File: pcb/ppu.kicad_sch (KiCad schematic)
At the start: 26 parts, among them IC6 AT25SF041B-SSHB-B, J10 Micro_SD_Card_Det2, Q8 MMBT2222A, U5 STM32U073CCUx, Y4 CM7V-T1A-32.768KHZ

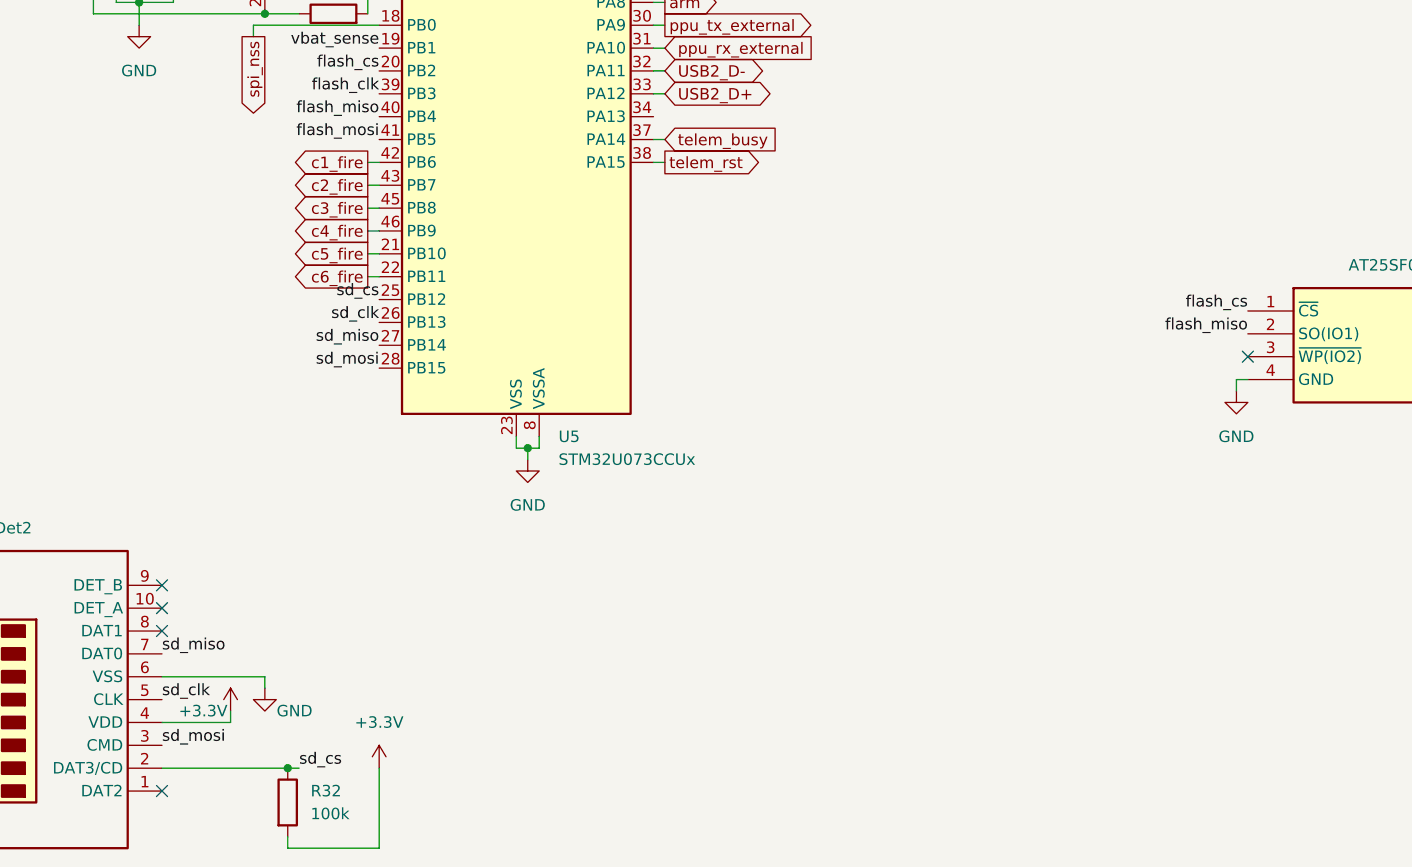
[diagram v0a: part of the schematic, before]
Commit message: lots of work on ppu firmware, especially relating to flash - also corrected some schematic errors (haven't gotten around to updating pcb yet)
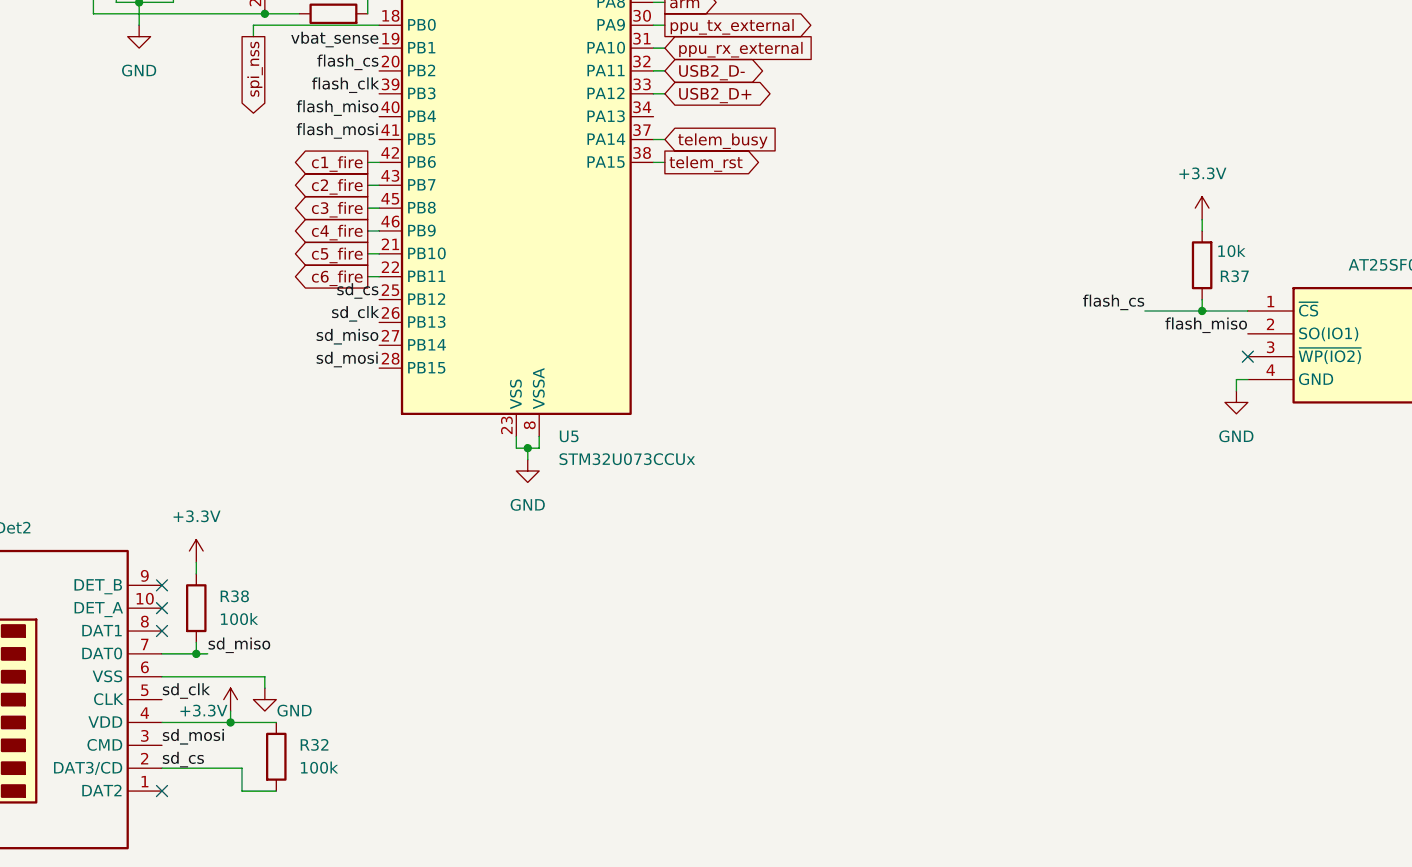
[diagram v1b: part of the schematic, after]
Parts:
- added R37: 10k, Resistor_SMD:R_0402_1005Metric, symbol Device:R
- added R38: 100k, Resistor_SMD:R_0402_1005Metric, symbol Device:R
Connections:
- net +3.3V: now also R32.1, R37.2, R38.1; no longer R32.2
- net flash_cs: now also R37.1
- net sd_cs: now also R32.2; no longer R32.1
- net sd_miso: now also R38.2
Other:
- moved on the sheet: R32

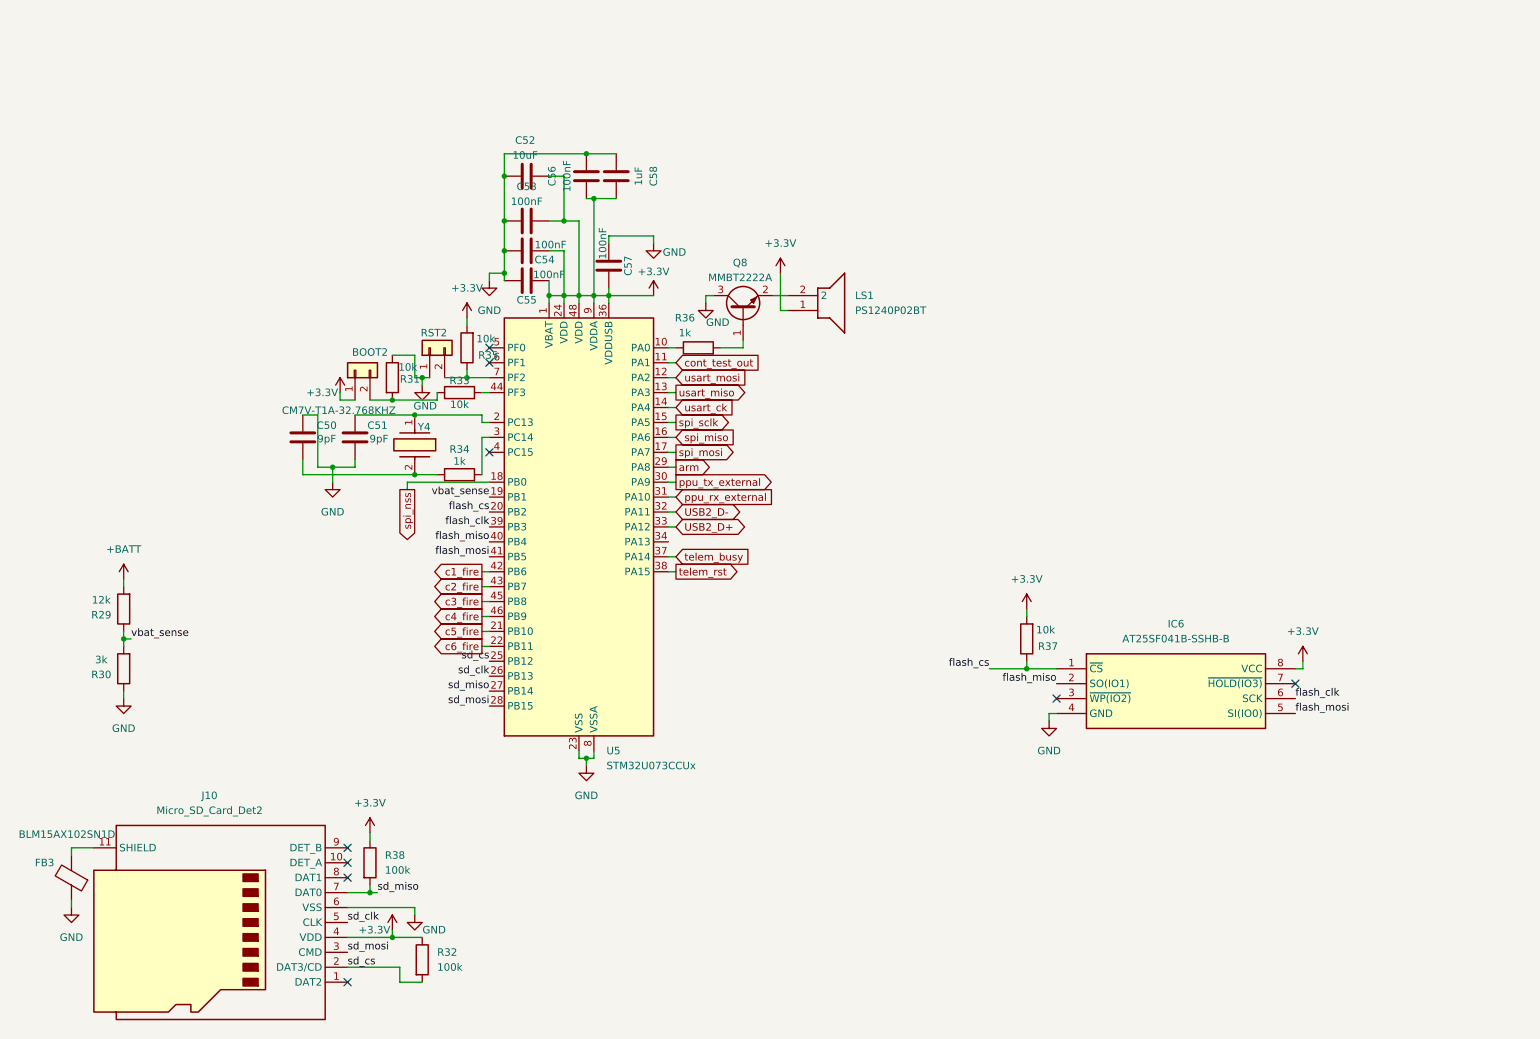
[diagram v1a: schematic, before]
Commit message: reorganized schematic, started to add a readme (not really though), also pcb updated
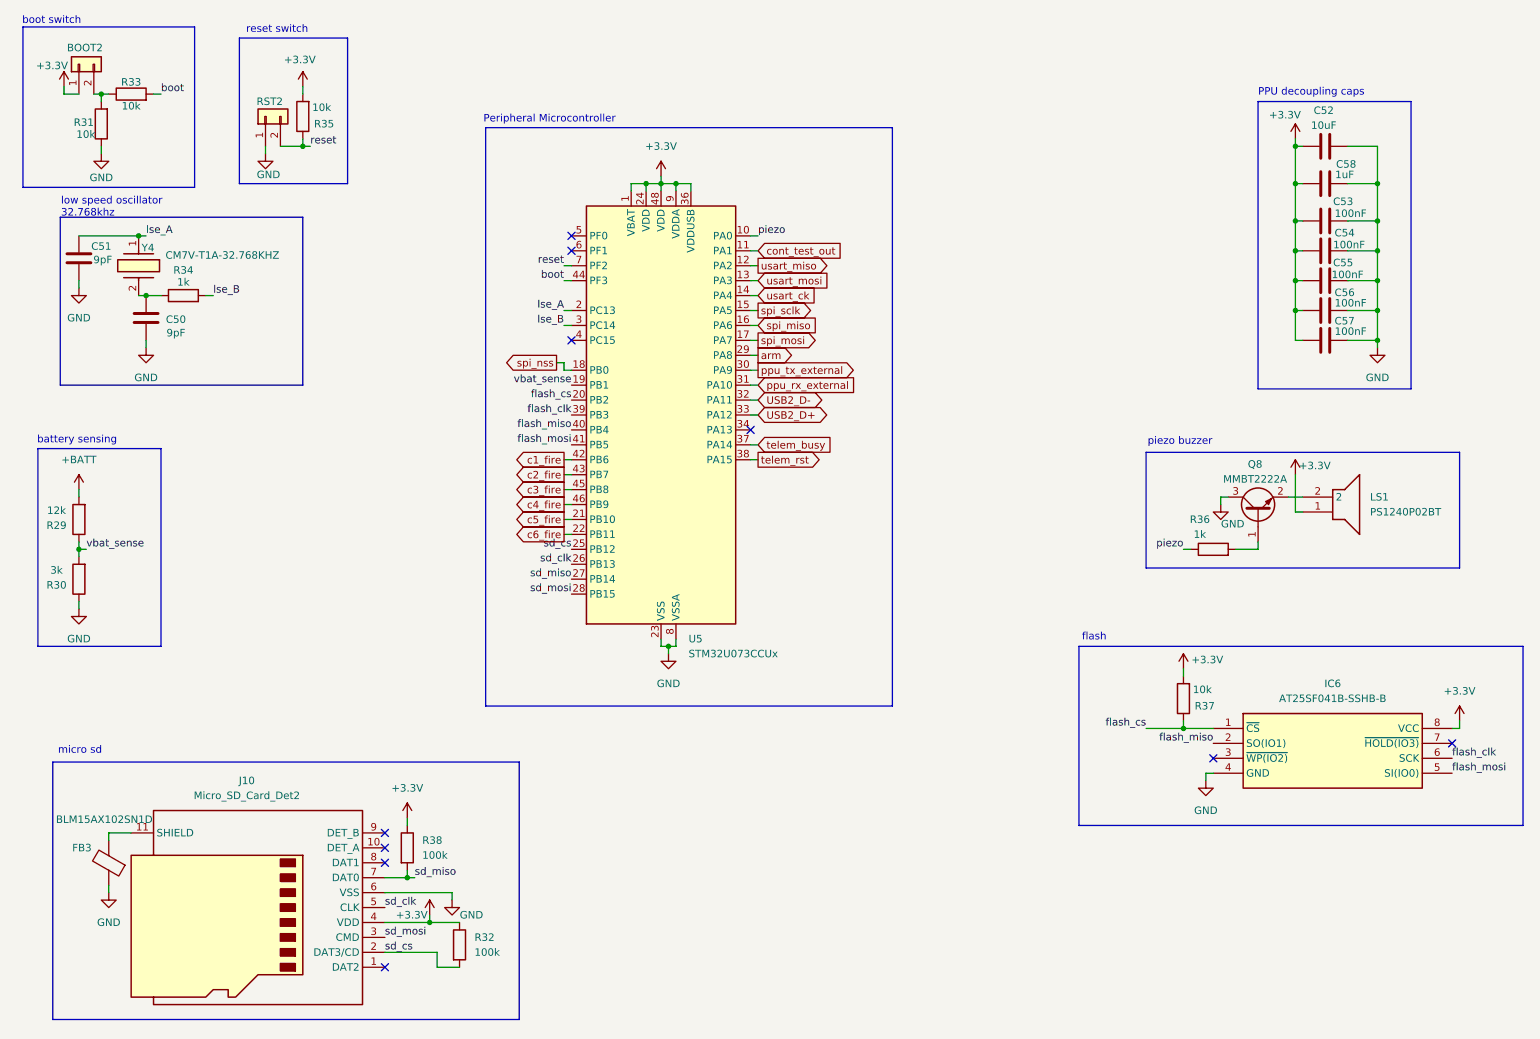
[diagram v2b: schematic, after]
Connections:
- net +3.3V: now also C52.1, C53.1, C54.2, C55.2, C56.2, C57.1, C58.1; no longer C52.2, C53.2, C54.1, C55.1, C56.1, C57.2, C58.2
- net GND: now also C50.2, C52.2, C53.2, C54.1, C55.1, C56.1, C57.2, C58.2; no longer C50.1, C52.1, C53.1, C54.2, C55.2, C56.2, C57.1, C58.1
- net usart_miso: now also U5.12 (PA2); no longer U5.13 (PA3)
- net usart_mosi: now also U5.13 (PA3); no longer U5.12 (PA2)
- net at R34.1, Y4.2: now also C50.1; no longer C50.2
- net reset: now reaches R35.1, RST2.2 (Pin_2), U5.7 (PF2)
- net lse_B: now reaches R34.2, U5.3 (PC14)
- net piezo: now reaches R36.1, U5.10 (PA0)
- net lse_A: now reaches C51.1, U5.2 (PC13), Y4.1
- net boot: now reaches R33.2, U5.44 (PF3)
- no-connect marks 9 -> 10
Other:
- note added: "PPU decoupling caps"
- note added: "Peripheral Microcontroller"
- note added: "battery sensing"
- note added: "boot switch"
- note added: "flash"
- note added: "low speed oscillator 32.768khz"
- note added: "micro sd"
- note added: "piezo buzzer"
- note added: "reset switch"
- moved on the sheet: BOOT2, C50, C51, C52, C53, C54, C55, C56, C57, C58, FB3, IC6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

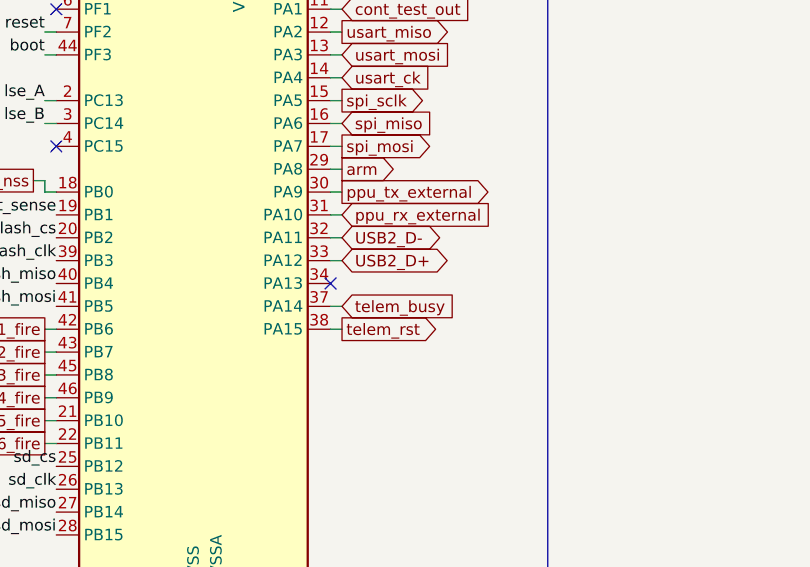
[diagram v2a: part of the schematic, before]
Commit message: added camera high side switching
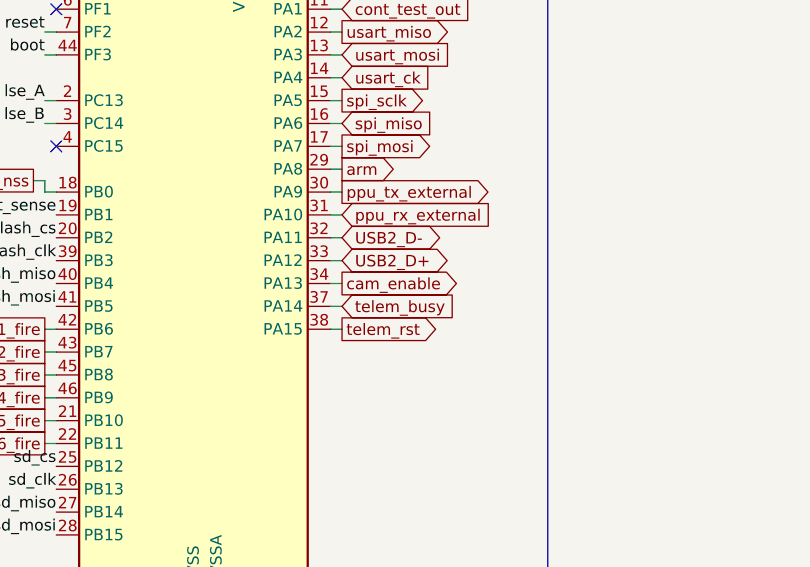
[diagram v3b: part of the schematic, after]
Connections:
- net cam_enable: now reaches U5.34 (PA13)
- no-connect marks 10 -> 9
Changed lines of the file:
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@@
-	)
-	(no_connect
-		(at 140.97 93.98)
 	)
 	(no_connect
@@
 		(pts
 			(xy 140.97 66.04) (xy 142.24 66.04)
+		)
+		(stroke
+			(width 0)
+			(type default)
+		)
+	)
+	(wire
+		(pts
+			(xy 140.97 93.98) (xy 142.24 93.98)
 		)
 		(stroke
@@
 			(effects
 				(font
+					(size 1.27 1.27)
+				)
+				(justify left)
+				(hide yes)
+			)
+		)
+	)
+	(global_label "cam_enable"
+		(shape output)
+		(at 142.24 93.98 0)
+		(fields_autoplaced yes)
+		(effects
+			(font
+				(size 1.27 1.27)
+			)
+			(justify left)
+		)
+		(property "Intersheetrefs" "${INTERSHEET_REFS}"
+			(at 156.4131 93.98 0)
+			(effects
+				(font

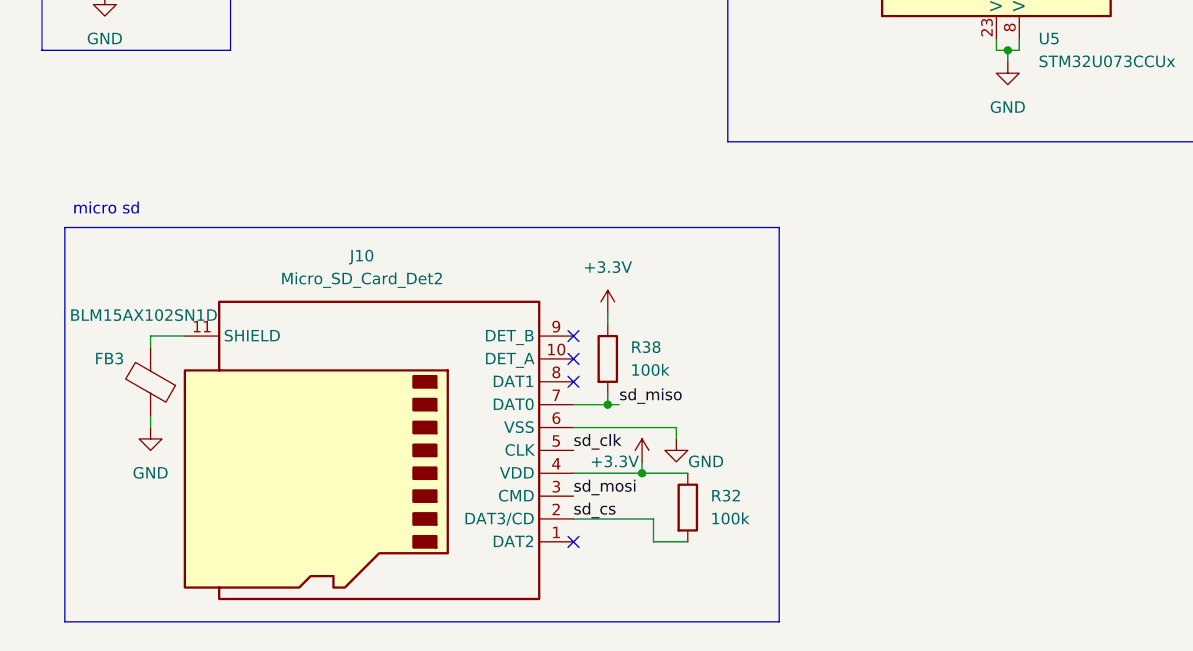
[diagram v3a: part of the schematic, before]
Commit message: fixed micro sd pullups
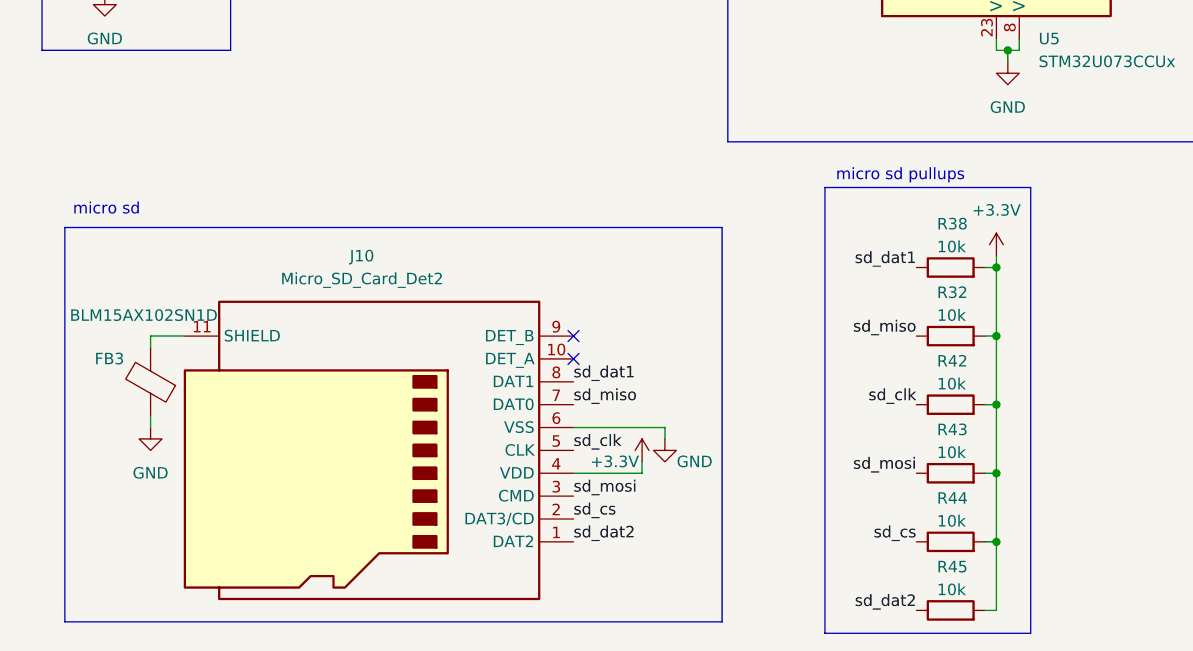
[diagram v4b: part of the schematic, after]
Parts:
- added R42, R43, R44, R45: 10k, Resistor_SMD:R_0402_1005Metric, symbol Device:R
- R32, R38: value 100k -> 10k
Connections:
- net +3.3V: now also R32.2, R38.2, R42.2, R43.2, R44.2, R45.2; no longer R32.1, R38.1
- net sd_clk: now also R42.1
- net sd_cs: now also R44.1; no longer R32.2
- net sd_miso: now also R32.1; no longer R38.2
- net sd_mosi: now also R43.1
- net sd_dat2: now reaches J10.1 (DAT2)
- net sd_dat2: now also R45.1
- net sd_dat1: now reaches J10.8 (DAT1)
- net sd_dat1: now also R38.1
- no-connect marks 9 -> 7
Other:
- note added: "micro sd pullups"
- moved on the sheet: R38
